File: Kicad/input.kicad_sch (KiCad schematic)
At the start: 8 parts, among them J1 AudioJack4, U4 OPA1656ID

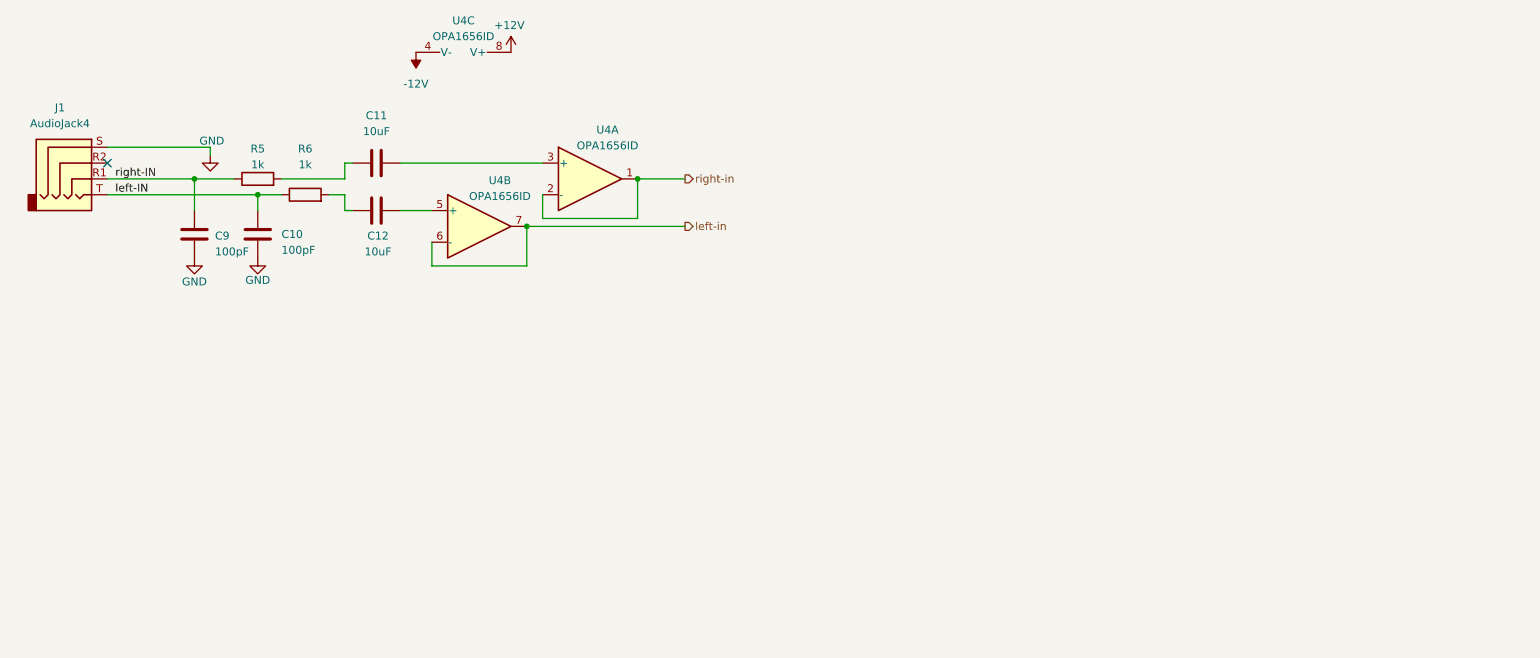
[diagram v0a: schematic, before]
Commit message: moved dac to input path and added input multiplexing
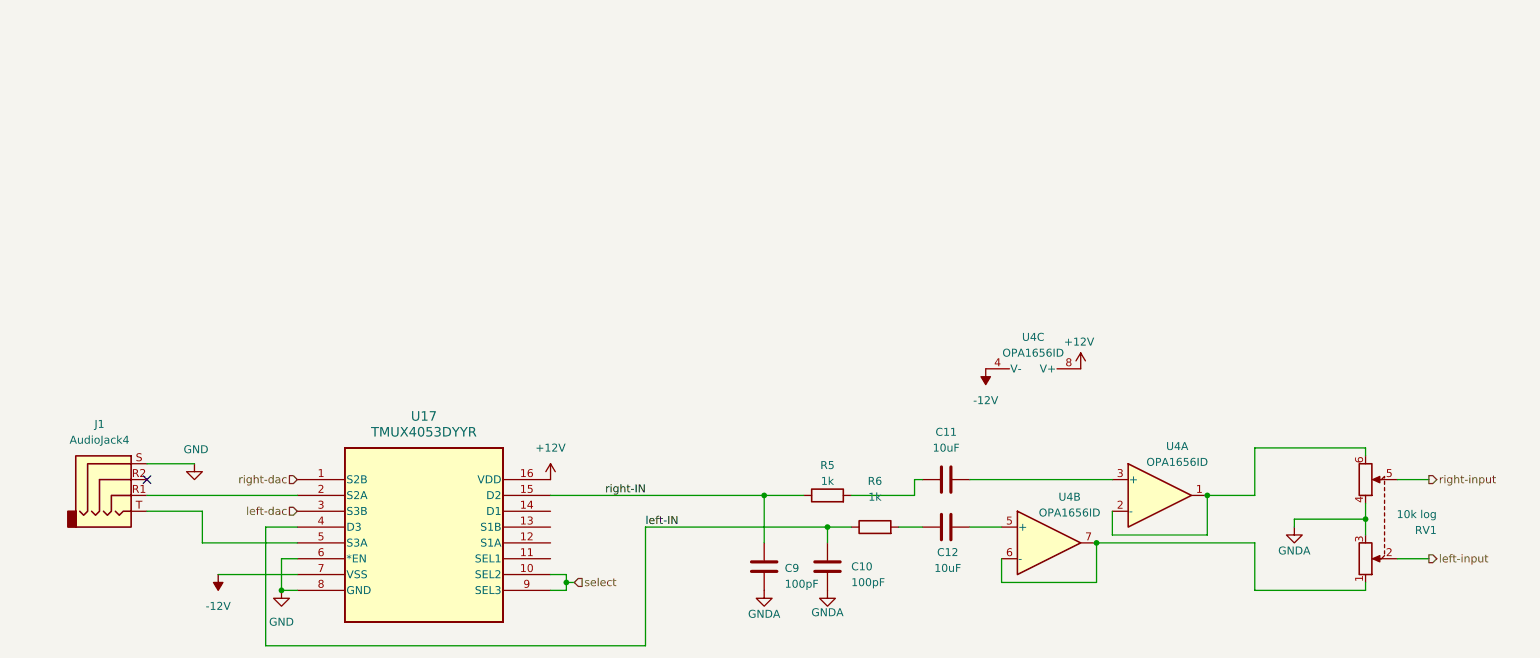
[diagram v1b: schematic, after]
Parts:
- added RV1: 10k log, Library:10k pot, symbol Device:R_Potentiometer_Dual
- added U17: TMUX4053DYYR, SOT-23-THIN16_DYY_TEX, symbol Symbols:TMUX4053DYYR
- R5, R6: footprint Capacitor_SMD:C_0805_2012Metric_Pad1.18x1.45mm_HandSolder -> Resistor_SMD:R_0805_2012Metric_Pad1.20x1.40mm_HandSolder
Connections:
- net +12V: now also U17.16 (VDD)
- net -12V: now also U17.7 (VSS)
- net GND: now also U17.6 (*EN), U17.8 (GND); no longer C10.2, C9.2
- net left-IN: now also U17.4 (D3); no longer J1.T
- net right-IN: now also U17.15 (D2); no longer J1.R1
- net left-in: no longer names the net of U4.6 (-), U4.7
- net left-in: now also RV1.1
- net right-in: no longer names the net of U4.1, U4.2 (-)
- net right-in: now also RV1.6
- new net: J1.R1, U17.2 (S2A)
- new net: J1.T, U17.5 (S3A)
- new net GNDA: C10.2, C9.2, RV1.3, RV1.4
- new net left-dac: U17.3 (S3B)
- new net left-input: RV1.2
- new net right-dac: U17.1 (S2B)
- new net right-input: RV1.5
- new net select: U17.10 (SEL2), U17.9 (SEL3)
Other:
- moved on the sheet: C10, C11, C12, C9, R5, R6, U4A, U4B, U4C

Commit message: final schematic
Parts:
- C11, C12: value 10uF -> 1uF
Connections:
- net GND: now also C10.2, C9.2
- net GNDA: no longer C10.2, C9.2
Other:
- moved on the sheet: C10, C11, C12, C9, J1, R5, R6, RV1, U17, U4A, U4B, U4C

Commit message: fixed issues in amp
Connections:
- net GNDA is gone; now on net GND: RV1.3, RV1.4
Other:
- moved on the sheet: C10, C11, C12, C9, R5, R6, RV1, U4A, U4B, U4C
